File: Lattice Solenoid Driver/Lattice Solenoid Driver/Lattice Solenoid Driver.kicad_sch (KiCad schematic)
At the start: 172 parts, among them U1 MCP23017_SS, U15 DRV8873SPWPR, U16 DRV8873SPWPR, U17 DRV8873SPWPR, U18 DRV8873SPWPR, U2 MCP23017_SS, U27 DRV8873SPWPR, U28 DRV8873SPWPR, U29 DRV8873SPWPR, U3 DRV8873SPWPR, U30 DRV8873SPWPR, U39 DRV8873SPWPR, U4 DRV8873SPWPR, U40 DRV8873SPWPR, U41 DRV8873SPWPR, U42 DRV8873SPWPR, U5 DRV8873SPWPR, U6 DRV8873SPWPR

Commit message: Rev1 mostly done
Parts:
- removed C10, C100, C101, C102, C15, C16, C17, C18, C35, C36, C37, C38, C43, C44, C45, C46, C63, C64, C65, C66, C7, C71, C72, C73, C74, C8, C9, C91, C92, C93, C94, C99: 100nF, Capacitor_SMD:C_0805_2012Metric, symbol Device:C
- removed C103, C104, C105, C106, C19, C20, C21, C22, C3, C31, C32, C33, C34, C4, C47, C48, C49, C5, C50, C59, C6, C60, C61, C62, C75, C76, C77, C78, C87, C88, C89, C90: 1uF, Capacitor_SMD:C_0805_2012Metric, symbol Device:C
- removed C107, C108, C109, C110, C111, C112, C113, C114, C23, C24, C25, C26, C27, C28, C29, C30, C51, C52, C53, C54, C55, C56, C57, C58, C79, C80, C81, C82, C83, C84, C85, C86: 10uF, Capacitor_SMD:C_0805_2012Metric, symbol Device:C
- removed C11, C12, C13, C14, C39, C40, C41, C42, C67, C68, C69, C70, C95, C96, C97, C98: 47nF, Capacitor_SMD:C_0805_2012Metric, symbol Device:C
- removed U10, U11, U12, U13, U14, U19, U20, U21, U22, U23, U24, U25, U26, U31, U32, U33, U34, U35, U36, U37, U38, U43, U44, U45, U46, U47, U48, U49, U50, U7, U8, U9: ~, symbol My_Library:30V_Supply
- removed U15, U16, U17, U18, U27, U28, U29, U3, U30, U39, U4, U40, U41, U42, U5, U6: DRV8873SPWPR, footprints:PWP24_TEX, symbol 2025-01-27_00-31-49:DRV8873SPWPR
- added H1, H2, H3, H4, H5, H6, H7, H8: MountingHole_Pad, MountingHole:MountingHole_3.2mm_M3_DIN965_Pad_TopBottom, symbol Mechanical:MountingHole_Pad
- added J1: Conn_01x06_Pin, Connector_PinHeader_2.54mm:PinHeader_1x06_P2.54mm_Vertical, symbol Connector:Conn_01x06_Pin
- added J2, J20, J21, J22, J23, J24, J25, J26, J27, J28, J29, J30, J31, J32, J33, J5: Conn_01x02_Pin, Connector_PinHeader_2.54mm:PinHeader_1x02_P2.54mm_Vertical, symbol Connector:Conn_01x02_Pin
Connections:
- net GND: now also H2.1, H5.1, H6.1, H7.1, H8.1, J1.1 (Pin_1)
- net SCL: now also J1.4 (Pin_4)
- net SDA: now also J1.3 (Pin_3)
- net VDD: now also J1.2 (Pin_2)
- new net 30V: H1.1
- new net H Bridge/SOL+: J2.2 (Pin_2)
- new net H Bridge/SOL-: J2.1 (Pin_1)
- new net H Bridge1/SOL+: J5.2 (Pin_2)
- new net H Bridge1/SOL-: J5.1 (Pin_1)
- new net H Bridge10/SOL+: J28.2 (Pin_2)
- new net H Bridge10/SOL-: J28.1 (Pin_1)
- new net H Bridge11/SOL+: J29.2 (Pin_2)
- new net H Bridge11/SOL-: J29.1 (Pin_1)
- new net H Bridge12/SOL+: J30.2 (Pin_2)
- new net H Bridge12/SOL-: J30.1 (Pin_1)
- new net H Bridge13/SOL+: J31.2 (Pin_2)
- new net H Bridge13/SOL-: J31.1 (Pin_1)
- new net H Bridge14/SOL+: J32.2 (Pin_2)
- new net H Bridge14/SOL-: J32.1 (Pin_1)
- new net H Bridge15/SOL+: J33.2 (Pin_2)
- new net H Bridge15/SOL-: J33.1 (Pin_1)
- new net H Bridge2/SOL+: J20.2 (Pin_2)
- new net H Bridge2/SOL-: J20.1 (Pin_1)
- new net H Bridge3/SOL+: J21.2 (Pin_2)
- new net H Bridge3/SOL-: J21.1 (Pin_1)
- new net H Bridge4/SOL+: J22.2 (Pin_2)
- new net H Bridge4/SOL-: J22.1 (Pin_1)
- new net H Bridge5/SOL+: J23.2 (Pin_2)
- new net H Bridge5/SOL-: J23.1 (Pin_1)
- new net H Bridge6/SOL+: J24.2 (Pin_2)
- new net H Bridge6/SOL-: J24.1 (Pin_1)
- new net H Bridge7/SOL+: J25.2 (Pin_2)
- new net H Bridge7/SOL-: J25.1 (Pin_1)
- new net H Bridge8/SOL+: J26.2 (Pin_2)
- new net H Bridge8/SOL-: J26.1 (Pin_1)
- new net H Bridge9/SOL+: J27.2 (Pin_2)
- new net H Bridge9/SOL-: J27.1 (Pin_1)
- new net LOAD EN: J1.5 (Pin_5)
- new net LOAD PH: J1.6 (Pin_6)
- new net Load Motor H Bridge/SOL+: H3.1
- new net Load Motor H Bridge/SOL-: H4.1
- no-connect marks 150 -> 6
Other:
- added sheet H Bridge (hbridge.kicad_sch)
- added sheet H Bridge1 (hbridge.kicad_sch)
- added sheet H Bridge10 (hbridge.kicad_sch)
- added sheet H Bridge11 (hbridge.kicad_sch)
- added sheet H Bridge12 (hbridge.kicad_sch)
- added sheet H Bridge13 (hbridge.kicad_sch)
- added sheet H Bridge14 (hbridge.kicad_sch)
- added sheet H Bridge15 (hbridge.kicad_sch)
- added sheet H Bridge2 (hbridge.kicad_sch)
- added sheet H Bridge3 (hbridge.kicad_sch)
- added sheet H Bridge4 (hbridge.kicad_sch)
- added sheet H Bridge5 (hbridge.kicad_sch)
- added sheet H Bridge6 (hbridge.kicad_sch)
- added sheet H Bridge7 (hbridge.kicad_sch)
- added sheet H Bridge8 (hbridge.kicad_sch)
- added sheet H Bridge9 (hbridge.kicad_sch)
- added sheet Load Motor H Bridge (hbridge.kicad_sch)
- note removed: "Solenoid Connectors"
- note removed: "TBA"

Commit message: Finished Rev 1 initial
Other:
- moved on the sheet: C1, C2, H1, H2, H3, H4, H5, H6, H7, H8, J1, J2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

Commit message: finishing touches
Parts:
- R1, R2: Part # 0805W8F4701T5E -> C17673
- U1, U2: Part # (none) -> C558584

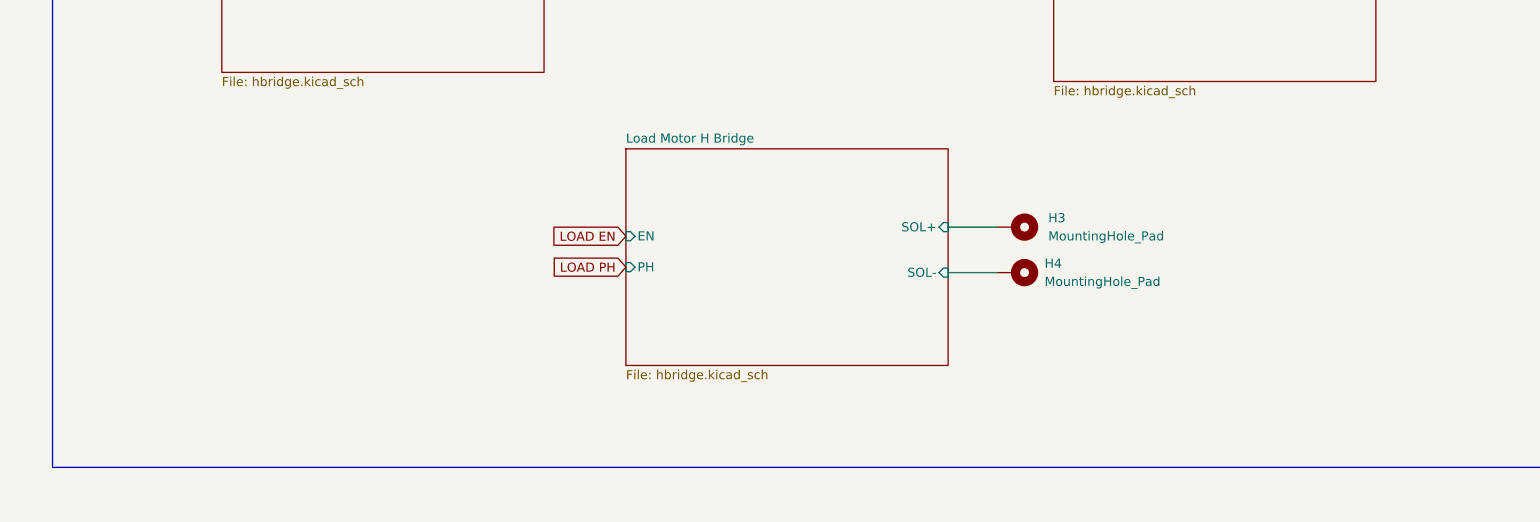
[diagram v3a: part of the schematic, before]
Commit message: adding stepper driver
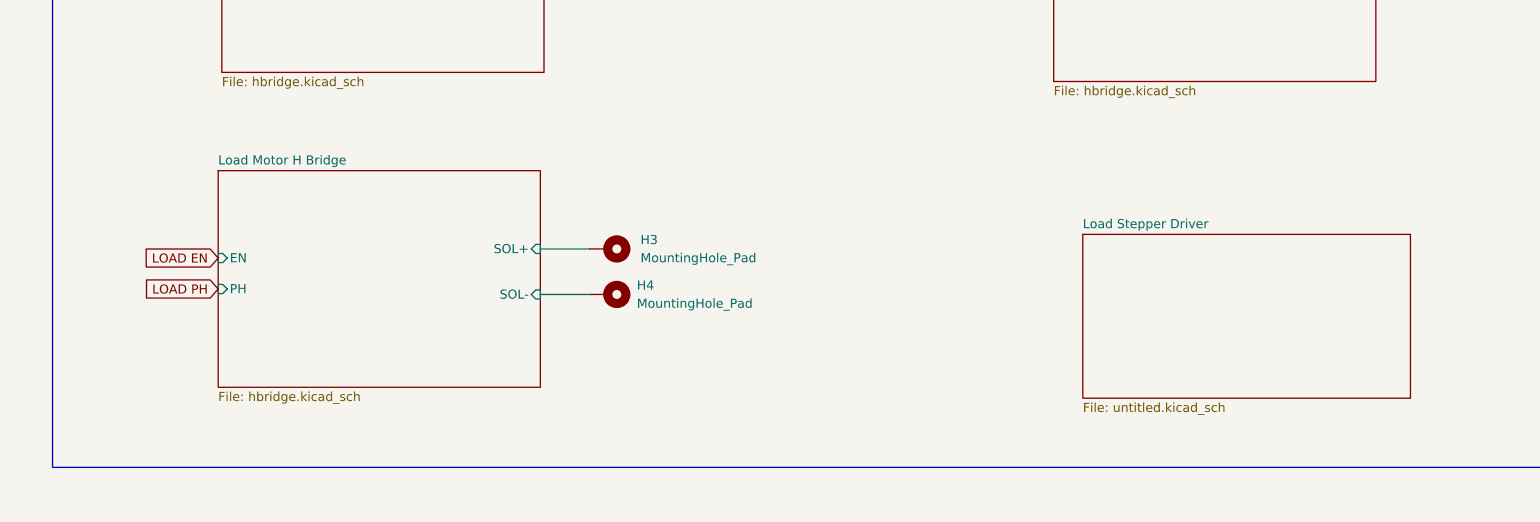
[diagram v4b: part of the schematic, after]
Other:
- added sheet Load Stepper Driver (untitled.kicad_sch)
- moved on the sheet: H3, H4
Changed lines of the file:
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@@
 	(wire
 		(pts
-			(xy 287.274 378.714) (xy 294.132 378.714)
+			(xy 230.378 381.762) (xy 237.236 381.762)
 		)
 		(stroke
@@
 	(wire
 		(pts
-			(xy 287.274 372.364) (xy 294.132 372.364)
+			(xy 230.378 375.412) (xy 237.236 375.412)
 		)
 		(stroke
@@
 	(global_label "LOAD PH"
 		(shape input)
-		(at 242.316 377.952 180)
+		(at 185.42 381 180)
 		(fields_autoplaced yes)
 		(effects
@@
 		)
 		(property "Intersheetrefs" "${INTERSHEET_REFS}"
-			(at 231.0455 377.952 0)
+			(at 174.1495 381 0)
 			(effects
 				(font
@@
 	(global_label "LOAD EN"
 		(shape input)
-		(at 242.316 373.634 180)
+		(at 185.42 376.682 180)
 		(fields_autoplaced yes)
 		(effects
@@
 		)
 		(property "Intersheetrefs" "${INTERSHEET_REFS}"
-			(at 231.1665 373.634 0)
+			(at 174.2705 376.682 0)
 			(effects
 				(font
@@
 	(symbol
 		(lib_id "Mechanical:MountingHole_Pad")
-		(at 296.672 378.714 270)
+		(at 239.776 381.762 270)
 		(unit 1)
 		(exclude_from_sim no)
@@
 		(fields_autoplaced yes)
 		(property "Reference" "H4"
-			(at 300.736 377.444 90)
+			(at 243.84 380.492 90)
 			(effects
 				(font
@@
 		)
 		(property "Value" "MountingHole_Pad"
-			(at 300.736 379.984 90)
+			(at 243.84 383.032 90)
 			(effects
 				(font
@@
 		)
 		(property "Footprint" "MountingHole:MountingHole_3.2mm_M3_DIN965_Pad_TopBottom"
-			(at 296.672 378.714 0)
+			(at 239.776 381.762 0)
 			(effects
 				(font
@@
 		)
 		(property "Datasheet" "~"
-			(at 296.672 378.714 0)
+			(at 239.776 381.762 0)
 			(effects
 				(font
@@
 		)
 		(property "Description" ""
-			(at 296.672 378.714 0)
+			(at 239.776 381.762 0)
 			(effects
 				(font
@@
 	(symbol
 		(lib_id "Mechanical:MountingHole_Pad")
-		(at 296.672 372.364 270)
+		(at 239.776 375.412 270)
 		(unit 1)
 		(exclude_from_sim no)
@@
 		(fields_autoplaced yes)
 		(property "Reference" "H3"
-			(at 301.244 371.094 90)
+			(at 244.348 374.142 90)
 			(effects
 				(font
@@
 		)
 		(property "Value" "MountingHole_Pad"
-			(at 301.244 373.634 90)
+			(at 244.348 376.682 90)
 			(effects
 				(font
@@
 		)
 		(property "Footprint" "MountingHole:MountingHole_3.2mm_M3_DIN965_Pad_TopBottom"
-			(at 296.672 372.364 0)
+			(at 239.776 375.412 0)
 			(effects
 				(font
@@
 		)
 		(property "Datasheet" "~"
-			(at 296.672 372.364 0)
+			(at 239.776 375.412 0)
 			(effects
 				(font
@@
 		)
 		(property "Description" ""
-			(at 296.672 372.364 0)
+			(at 239.776 375.412 0)
 			(effects
 				(font
@@
 	)
 	(sheet
-		(at 242.316 361.442)
+		(at 185.42 364.49)
 		(size 44.958 30.226)
 		(exclude_from_sim no)
@@
 		)
 		(property "Sheetname" "Load Motor H Bridge"
-			(at 242.316 360.7304 0)
+			(at 185.42 363.7784 0)
 			(effects
 				(font
@@
 		)
 		(property "Sheetfile" "hbridge.kicad_sch"
-			(at 242.316 392.2526 0)
+			(at 185.42 395.3006 0)
 			(effects
 				(font
@@
 		)
 		(pin "EN" input
-			(at 242.316 373.634 180)
+			(at 185.42 376.682 180)
 			(effects
 				(font
@@
 		)
 		(pin "PH" input
-			(at 242.316 377.952 180)
+			(at 185.42 381 180)
 			(effects
 				(font
@@
 		)
 		(pin "SOL+" input
-			(at 287.274 372.364 0)
+			(at 230.378 375.412 0)
 			(effects
 				(font
@@
 		)
 		(pin "SOL-" input
-			(at 287.274 378.714 0)
+			(at 230.378 381.762 0)
 			(effects
 				(font
@@
 				)
 			)
+		)
+	)
+	(sheet
+		(at 306.07 373.38)
+		(size 45.72 22.86)
+		(exclude_from_sim no)
+		(in_bom yes)
+		(on_board yes)
+		(dnp no)
+		(fields_autoplaced yes)
+		(stroke
+			(width 0.1524)
+			(type solid)
+		)
+		(fill
+			(color 0 0 0 0.0000)
+		)
+		(property "Sheetname" "Load Stepper Driver"
+			(at 306.07 372.6684 0)
+			(effects
+				(font
+					(size 1.27 1.27)
+				)
+				(justify left bottom)
+			)
+		)
+		(property "Sheetfile" "untitled.kicad_sch"
+			(at 306.07 396.8246 0)
+			(effects
+				(font
+					(size 1.27 1.27)
+				)
+				(justify left top)
+			)
+		)
+		(instances
+			(project "Lattice Solenoid Driver"
+				(path "/dd3049f9-60ef-48df-858e-65109e262c3c"
+					(page "19")
+				)
+			)

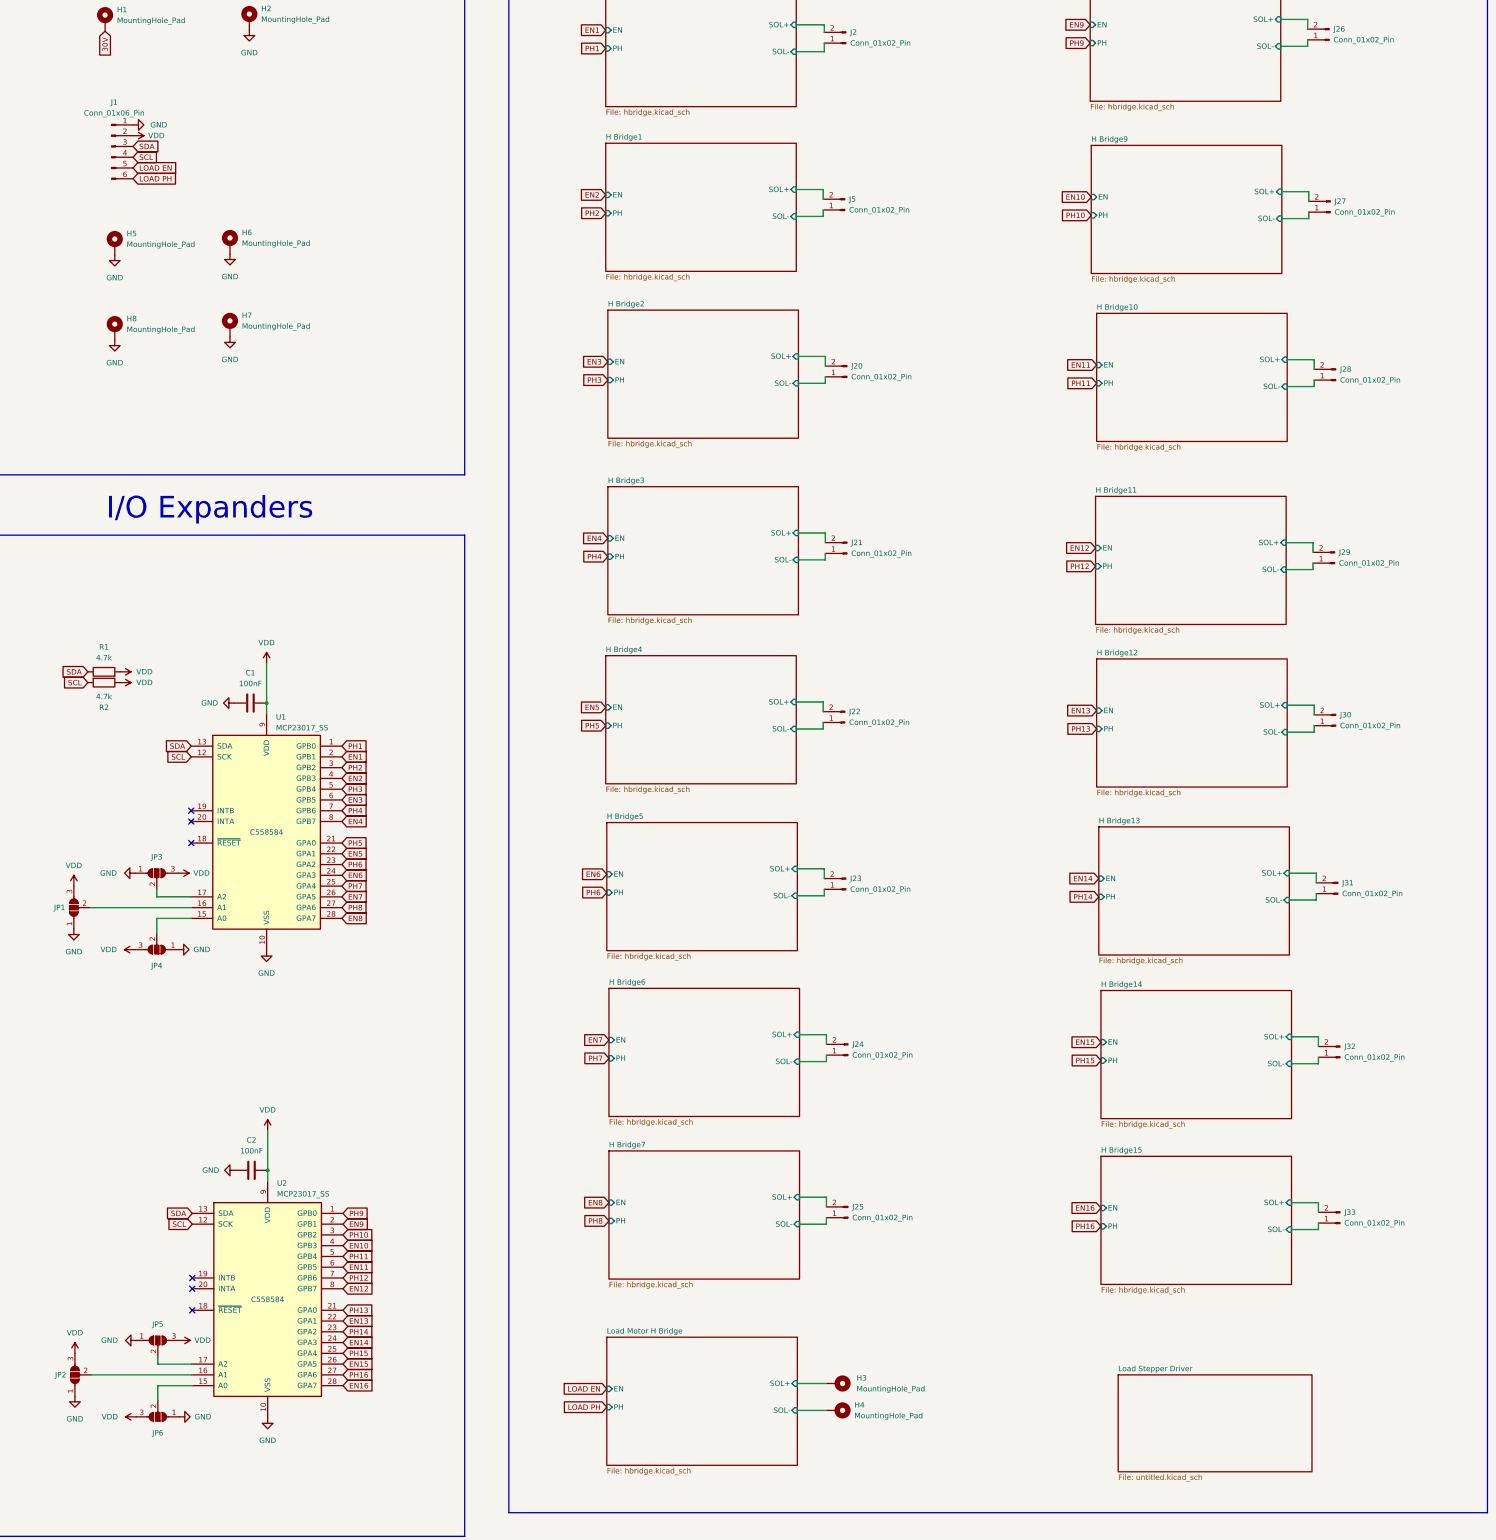
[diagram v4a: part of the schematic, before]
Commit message: added stepper sch
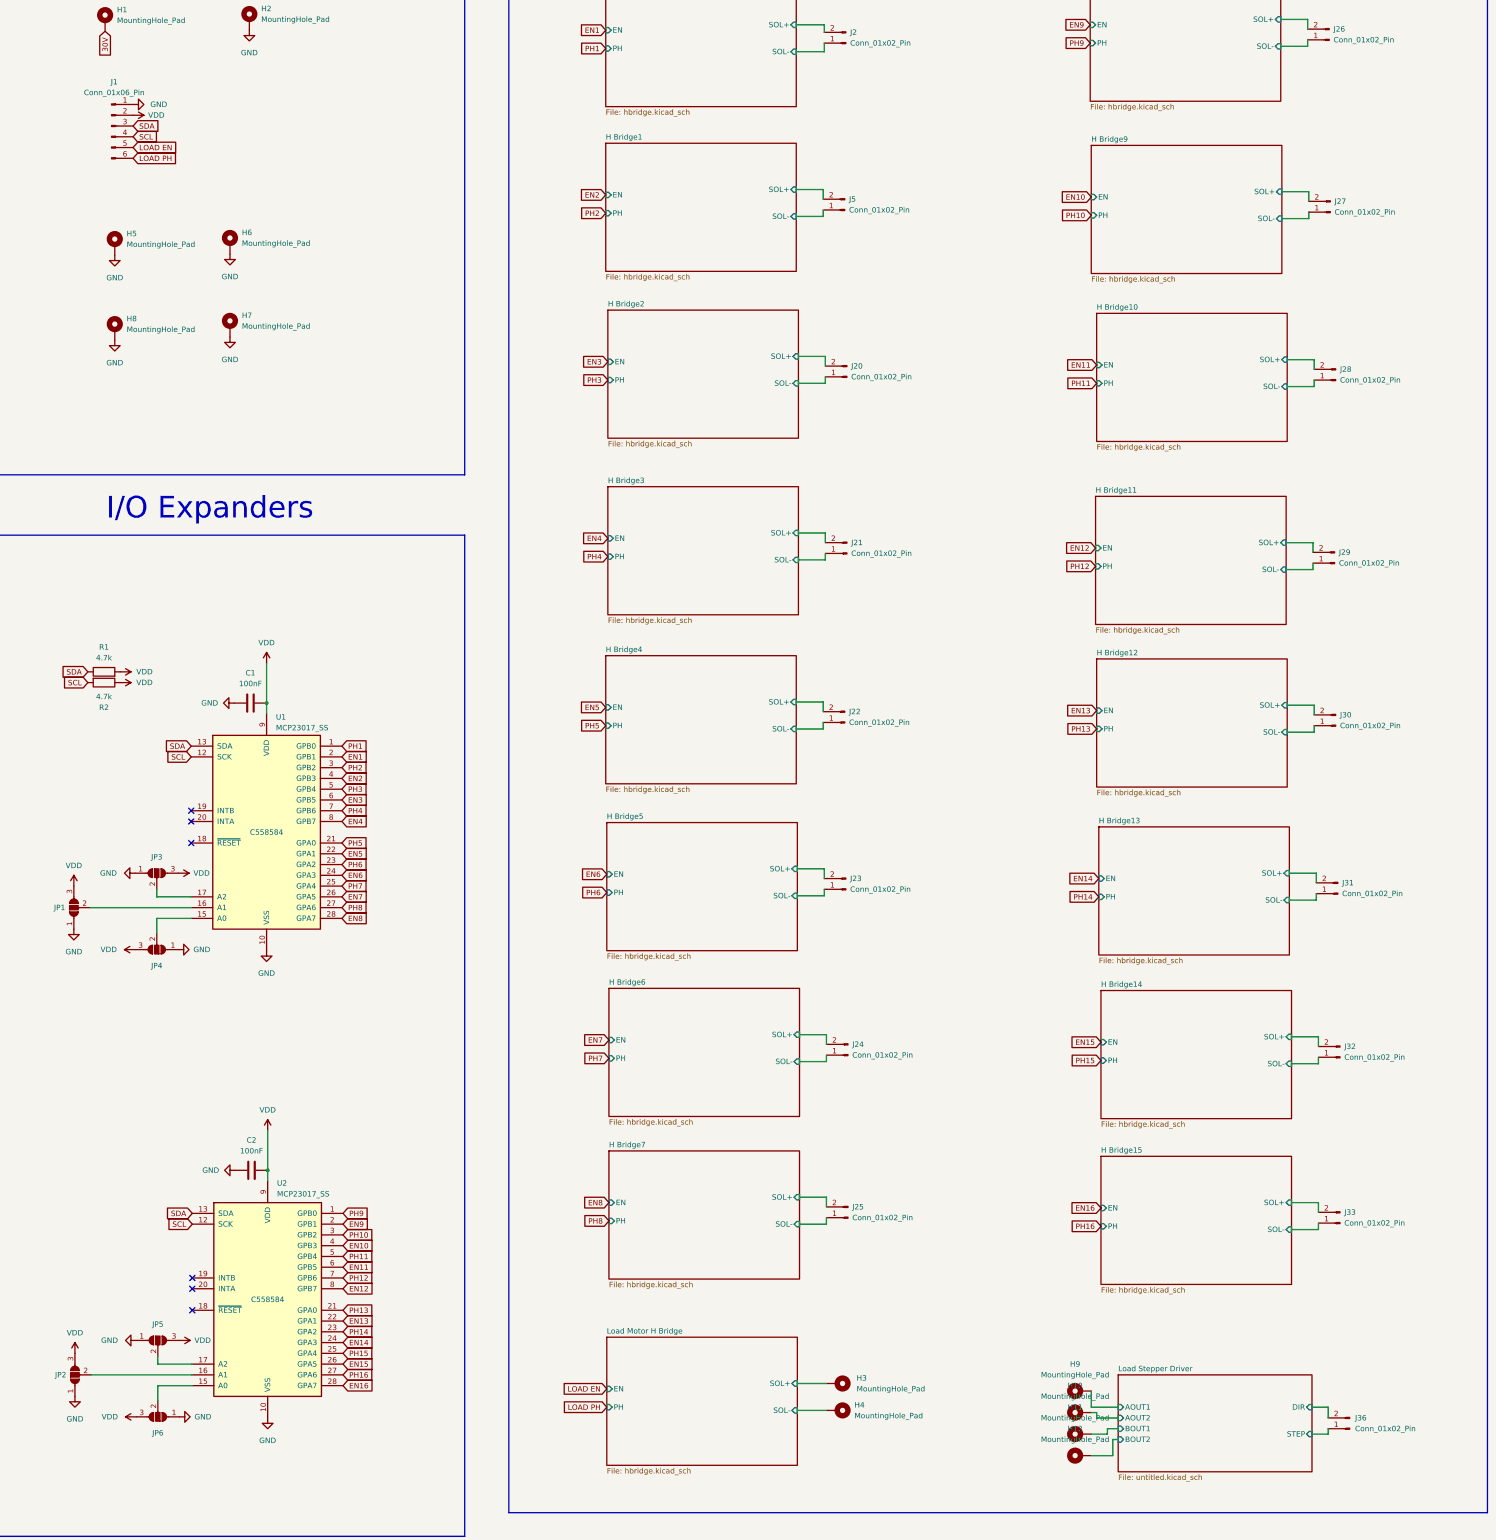
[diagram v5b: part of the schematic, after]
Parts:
- added H10, H11, H12, H9: MountingHole_Pad, MountingHole:MountingHole_3.2mm_M3_DIN965_Pad_TopBottom, symbol Mechanical:MountingHole_Pad
- added J36: Conn_01x02_Pin, Connector_PinHeader_2.54mm:PinHeader_1x02_P2.54mm_Vertical, symbol Connector:Conn_01x02_Pin
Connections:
- new net Load Stepper Driver/AOUT1: H9.1
- new net Load Stepper Driver/AOUT2: H10.1
- new net Load Stepper Driver/BOUT1: H11.1
- new net Load Stepper Driver/BOUT2: H12.1
- new net Load Stepper Driver/DIR: J36.2 (Pin_2)
- new net Load Stepper Driver/STEP: J36.1 (Pin_1)
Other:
- sheet Load Stepper Driver ports: added AOUT1, AOUT2, BOUT1, BOUT2, DIR, STEP; removed none
- moved on the sheet: J1
